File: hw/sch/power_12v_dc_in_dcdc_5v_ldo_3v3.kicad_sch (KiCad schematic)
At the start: 9 parts, among them J12 J_12V_IN, U2 DCDC_12V_3V3, U4 BAT54C

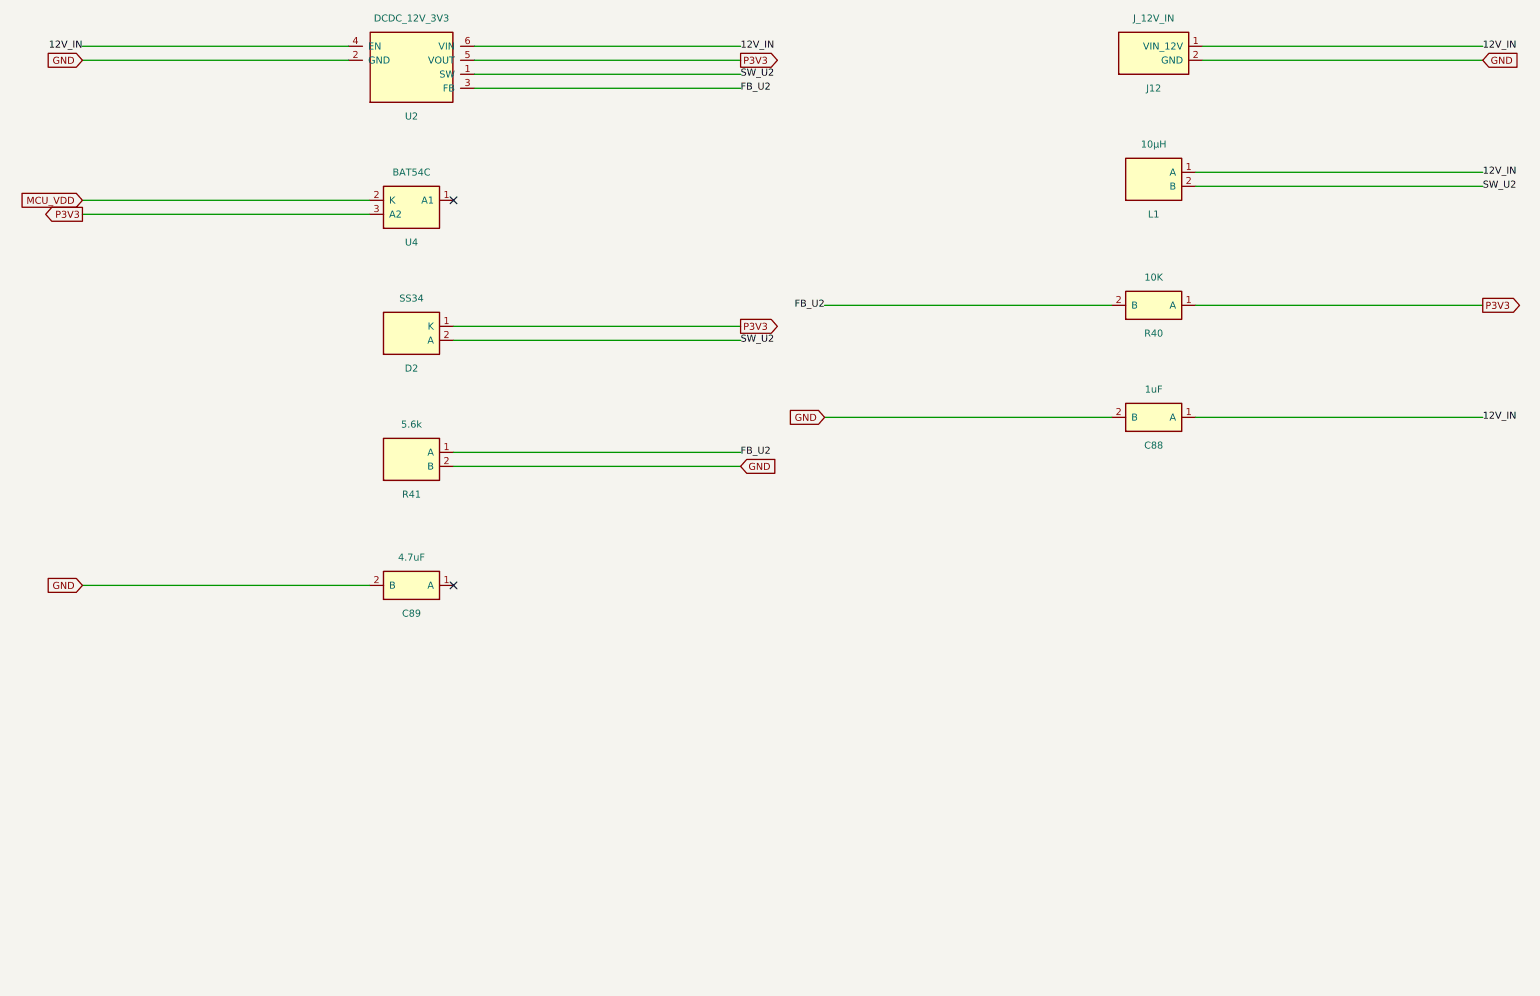
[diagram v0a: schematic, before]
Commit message: p4(k2): owner ⑤ 执行（#K2-24）—— 删 C89 + PWR_5V_KEY，7 载体一次做净
真源 bump（新件 errata-2 61c4694e：nets 101→100 / GND 211→210 / placements 55→54；原件 dd794c54 不动）
SPEC bump rev-50 ed0950687e5aec97（深 diff 断言：low_speed_nets 19→18 · power_pad_connect.entries 185→184
  · live board_sha16×3+basis（6ff49da5→dae8dc8d）· 新增 _spec_rev_50；retired_superseded_* 两条按红线留存）
pro 35c8f34bde7ac00c（netclass_assignments 146→145，文本级 3 行）· BOM db081546bbe64c37（54 refs）
受审板 l5 6ff49da5678c2108→dae8dc8d48ff5b81（删 C89 fps59→58 + GND 短段 + 端点缝合 via + 孤网 PWR_5V_KEY）
原理图 1 件 cb3c2134→dbaa989e（其余 5 件逐字节同；符号库未变）· project.yaml 56583331599fab0f（spec_name rev-50 / nets_yaml errata-2）
图集 v11 e284e9afd9054408（55→54 件；01/02/05 变，03/04/06/07 未漂）· 落位解逐字节不变（C89 不在 15 件解内，具名）

守恒闸：未连接 0 · DRC 类型集不增（73=39courtyard+34lib_mismatch；沙箱 lib_footprint_issues 已由同址对照臂证为位置伪差）
  · 非 45° 0/4720 · 阻抗/等长/走廊不退化（SPEC 深 diff + 图集 C4/C6/D1 pass + refplane 逐值同前）· 冻结四源不变
判定器：PASS 7 / FAIL 3（集合同名；net_declared_realized「<2 焊盘」1→0；refdes 55/59→54/58）
⚠️ 生成器一项未达（具名上报，未改）：k2_gen_v5.py 的 K2_REFS 取自冻结锚板（:54/:68-77/:79，断言 :830-835）⇒
  ❌ 写盘阻断 [YAML] ... 不存在 ref: ['C89']；最小补丁提案（K2_REFS 改读真源 YAML）须监理批
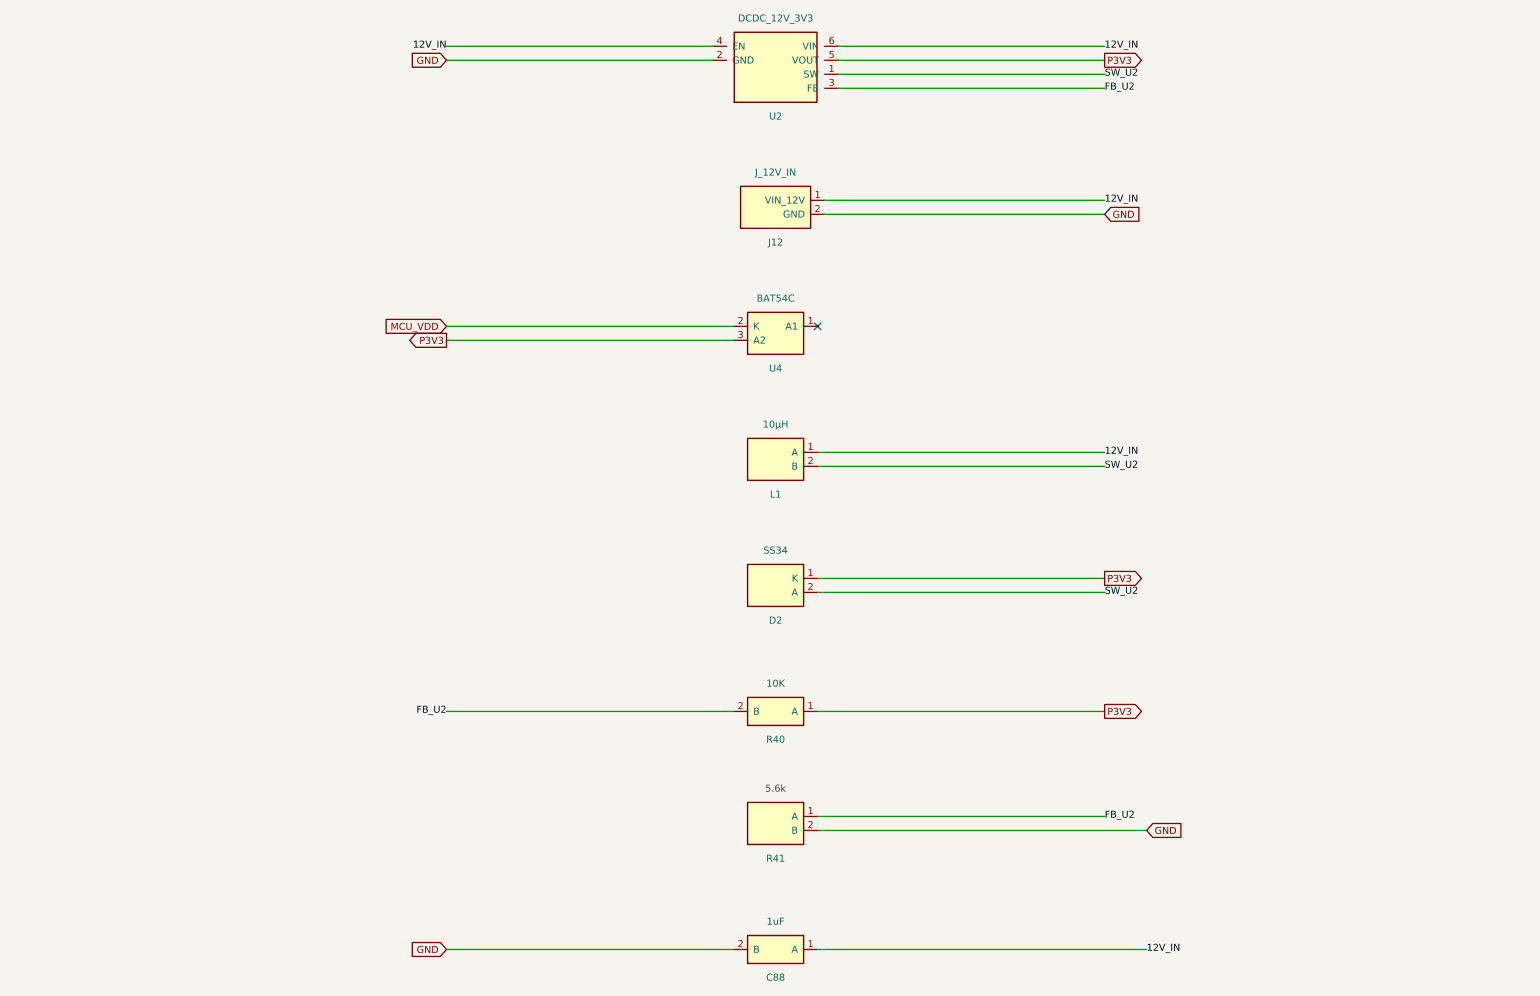
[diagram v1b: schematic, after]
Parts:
- removed C89: 4.7uF, Capacitor_SMD:C_0603_1608Metric, symbol IOCONVERT:C_4R7
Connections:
- no-connect marks 2 -> 1
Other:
- moved on the sheet: C88, D2, J12, L1, R40, R41, U2, U4

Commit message: fix(K2/#K2-57 R1+R2+R3+R4+R5+R6): CR-26 U4 BAT54C ORing 反接修复链落地 (新 rev 前置) + CR-27 并入 + 引证 5 项 + CR-32/CR-33 在册
R1(真源·四树): BAT54C.yaml 1:A1/2:A2/3:K (另笔于 _shared 四树)
R3(新 rev 前置·网表): 新增 hw/data/k2_sch.errata-3.yaml -- 仅订正 pin NAME->NUMBER
  BAT54C_ORING K 2->3 / A2 3->2 ; LED A 1->2 / K 2->1
  nets 逐字不动(100); k2_sch.yaml 逐字节未改 (dd794c54f7ce7417 => 判据 ④)
  pm_gate/project.yaml + pipeline.yaml nets_yaml -> errata-3 (版本 bump, 同 owner #K2-24 先例)
R2(符号层·有效杠杆澄清): IOCONVERT.kicad_sym#BAT54C_ORING -> K=3/A2=2;
  内嵌 sch (power_12v_...) 同步; 见 CR-33
R4(CR-27 并入): IOCONVERT.kicad_sym#LED -> A=2/K=1 + mcu_sideband.kicad_sch 同步
  (前置: 本机官方 LED_0603_1608Metric pad1 左侧 x=-0.7875, 阴极丝印 x=-1.485 => pad1=K)
R5(引证): 见 _shared 四树笔
R6(过程口径): CR-32 在册 (待裁项须结构化, 禁只写 handoff/ledger)

复算证据 (k2_gen_v5 双跑对照):
  errata-2: U4 pad2=MCU_VDD / pad3=P3V3   (复现缺陷)
  errata-3: U4 pad2=P3V3   / pad3=MCU_VDD (实体 A2->P3V3, K->MCU_VDD => 正向导通) OK
            D1 pad1=GND    / pad2=LED_A   (正向) OK
gate: sch_structural/netlist_connect/bom_consistent/project_sch_coverage 全 PASS
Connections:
- net MCU_VDD: now also U4.3 (K); no longer U4.2 (K)
- net P3V3: now also U4.2 (A2); no longer U4.3 (A2)
